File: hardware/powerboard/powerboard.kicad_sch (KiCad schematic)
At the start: 66 parts, among them J1 USB_B_Micro, J2 Boot, J3 Power, J4 Display, J5 Debug, J6 SPI_1, J7 I2C_0, J8 I2C_1, J9 UART_0, SW1 Oct_Up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

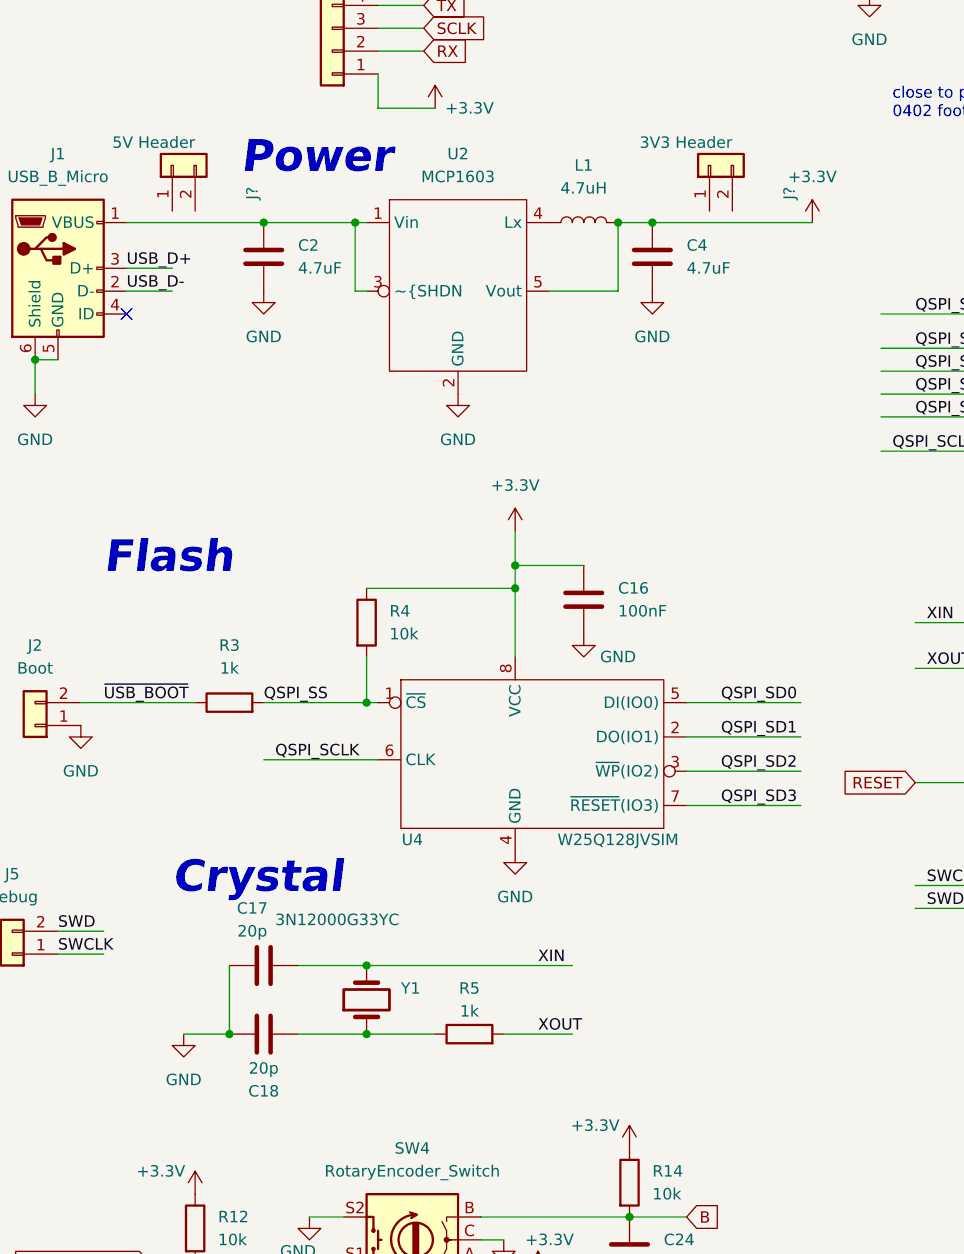
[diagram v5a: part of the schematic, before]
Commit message: Powerboard Finalization
Crystal Footprint and layout changed to match new crystal
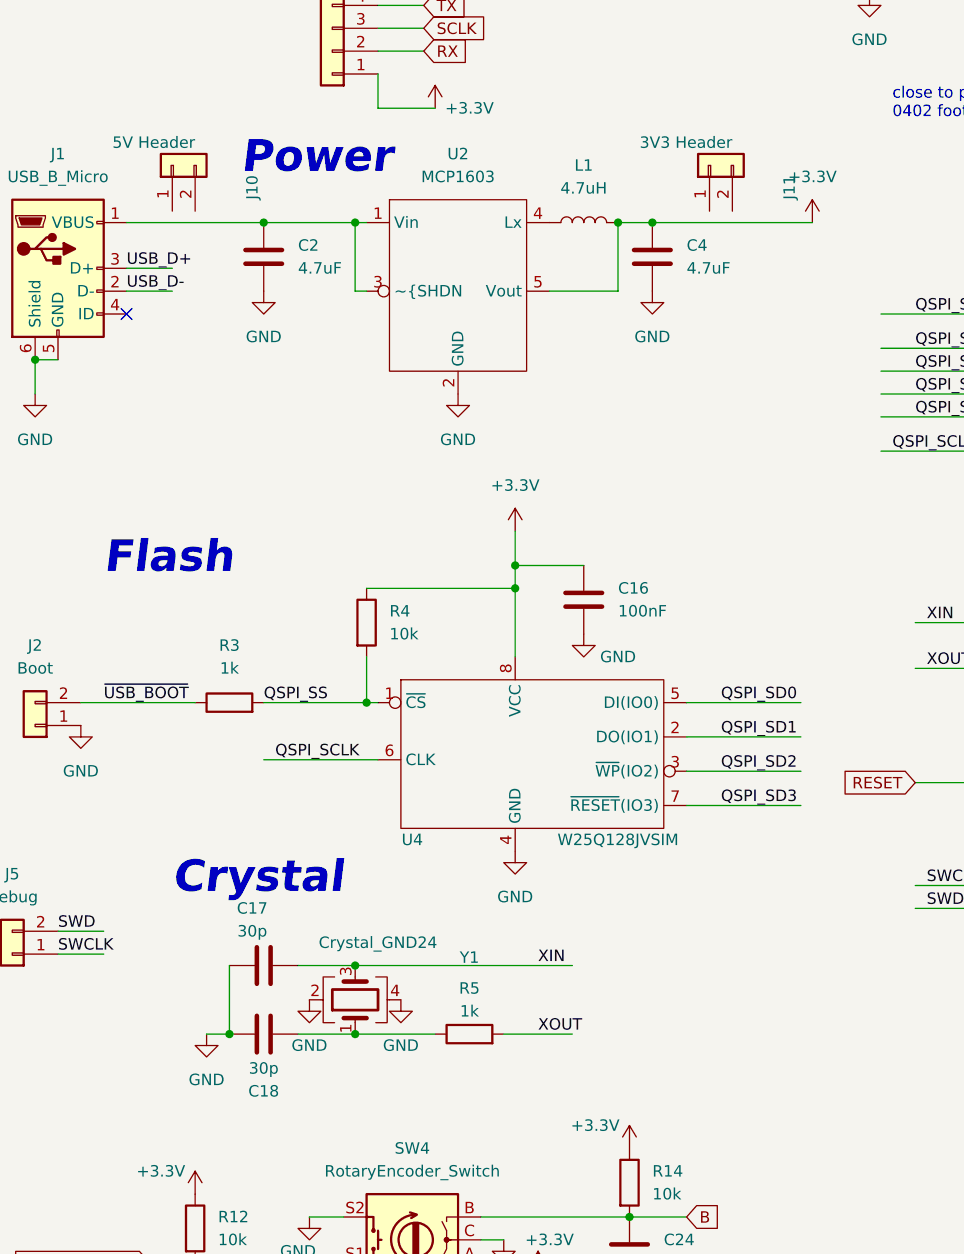
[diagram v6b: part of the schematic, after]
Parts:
- removed Y1: 3N12000G33YC, Crystal:Crystal_SMD_3225-4Pin_3.2x2.5mm, symbol Device:Crystal
- added Y1: Crystal_GND24, Crystal:Crystal_SMD_3225-4Pin_3.2x2.5mm, symbol Device:Crystal_GND24
- C17, C18: value 20p -> 30p
- gave numbers to parts that had none: 2
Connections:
- net GND: now also Y1.2, Y1.4
- net XIN: now also Y1.3
- net at C18.2, R5.1: now also Y1.1

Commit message: Powerboard review with sheaff
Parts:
- removed J7: I2C_0, Connector_PinHeader_2.54mm:PinHeader_1x02_P2.54mm_Vertical, symbol Connector_Generic:Conn_01x02
- removed J8: I2C_1, Connector_PinHeader_2.54mm:PinHeader_1x02_P2.54mm_Vertical, symbol Connector_Generic:Conn_01x02
- removed J9: UART_0, Connector_PinHeader_2.54mm:PinHeader_1x02_P2.54mm_Vertical, symbol Connector_Generic:Conn_01x02
- added J7: UART_0, Connector_PinSocket_2.54mm:PinSocket_1x03_P2.54mm_Vertical, symbol Connector_Generic:Conn_01x03
- added J8: I2C_0, Connector_PinSocket_2.54mm:PinSocket_1x04_P2.54mm_Vertical, symbol Connector_Generic:Conn_01x04
- J10, J11: footprint Connector_PinHeader_2.54mm:PinHeader_1x02_P2.54mm_Horizontal -> Connector_PinHeader_2.54mm:PinHeader_1x02_P2.54mm_Vertical
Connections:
- net +3.3V: now also J11.2 (Pin_2), J8.4 (Pin_4); no longer C4.1, L1.2, U2.5 (Vout)
- net GND: now also J7.1 (Pin_1), J8.3 (Pin_3)
- net SCL_0: now also J8.2 (Pin_2)
- net SDA_0: now also J8.1 (Pin_1)
- net UART_RX_0: now also J7.3 (Pin_3)
- net UART_TX_0: now also J7.2 (Pin_2)
- net at C2.1, U2.1 (Vin), U2.3 (~{SHDN): now also J10.2 (Pin_2); no longer J1.1 (VBUS)
- net at J10.1 (Pin_1): now also J1.1 (VBUS)
- net at J11.1 (Pin_1): now also C4.1, L1.2, U2.5 (Vout)
- net SCL_1: no longer names the net of U3.30 (GPIO19)
- net SDA_1: no longer names the net of U3.29 (GPIO18)
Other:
- moved on the sheet: J10, J11, J6

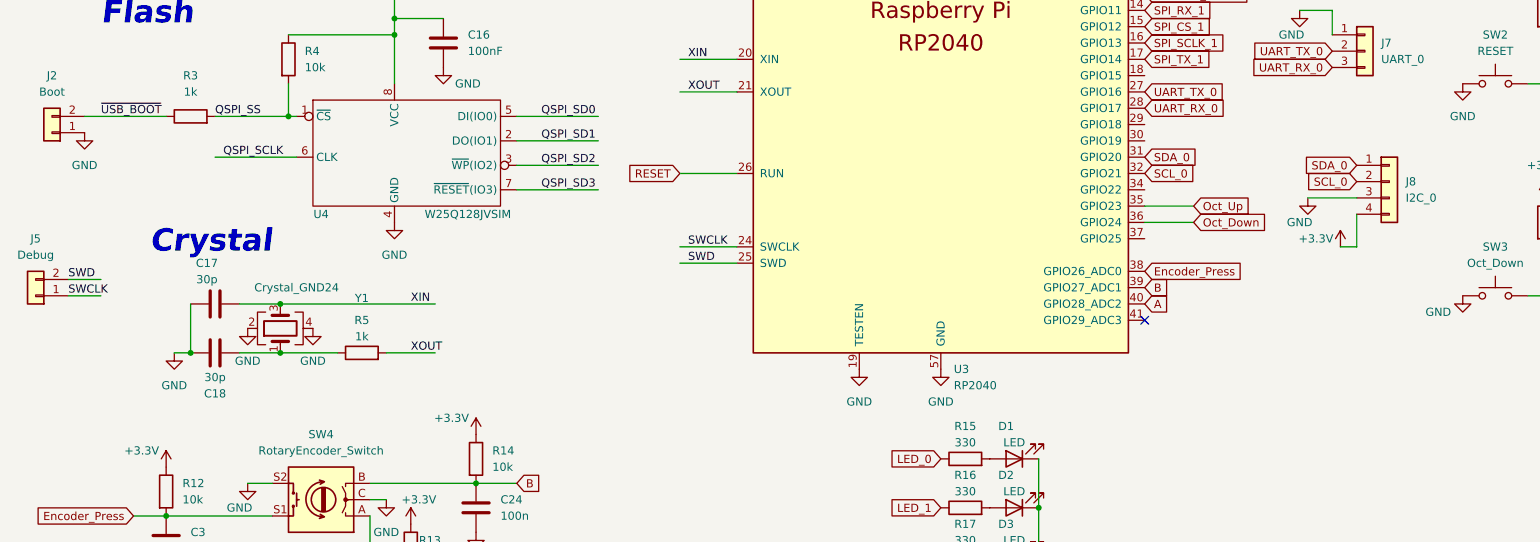
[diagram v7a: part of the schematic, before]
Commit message: Powerboard PCB Revisions
Expanded I2C Headers to include 3.3V and GND
Expanded UART Header to include GND
Expanded SWD Header to include GND
Added Silkscreen for All(?) Parts
Added GND Fill on Back Layer
Added header for 3.3V and 5V Current Measurements
Powerboard has all parts picked out and ready to order on JLC
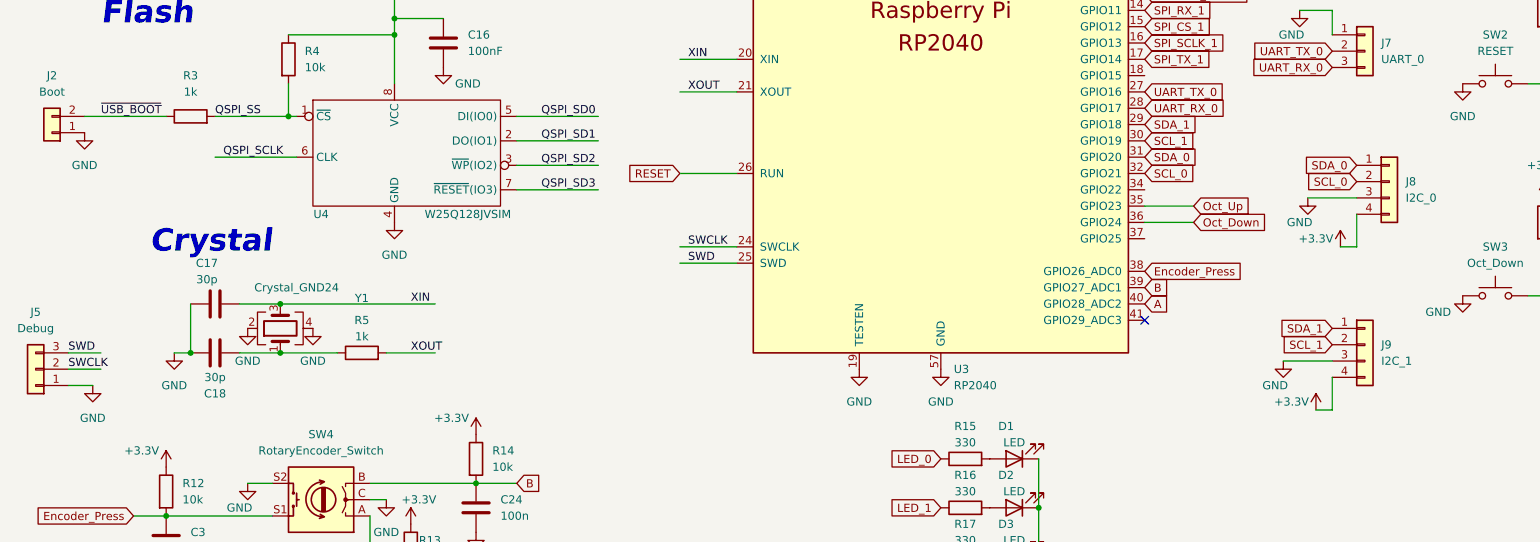
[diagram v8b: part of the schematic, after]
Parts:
- removed J5: Debug, Connector_PinSocket_2.54mm:PinSocket_1x02_P2.54mm_Vertical, symbol Connector_Generic:Conn_01x02
- added J5: Debug, Connector_PinHeader_2.54mm:PinHeader_1x03_P2.54mm_Vertical, symbol Connector_Generic:Conn_01x03
- added J9: I2C_1, Connector_PinSocket_2.54mm:PinSocket_1x04_P2.54mm_Vertical, symbol Connector_Generic:Conn_01x04
- R12: footprint Resistor_SMD:R_0402_1005Metric -> Resistor_SMD:R_0603_1608Metric
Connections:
- net +3.3V: now also J9.4 (Pin_4)
- net GND: now also J5.1 (Pin_1), J9.3 (Pin_3)
- net SWCLK: now also J5.2 (Pin_2)
- net SWD: now also J5.3 (Pin_3)
- net SDA_1: now reaches U3.29 (GPIO18)
- net SDA_1: now also J9.1 (Pin_1)
- net SCL_1: now reaches U3.30 (GPIO19)
- net SCL_1: now also J9.2 (Pin_2)
